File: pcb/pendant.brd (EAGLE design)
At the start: 24 x 99 mm, 47 parts, among them CON1 USB_MICROSMT+THRUHULE, Q2 16MHz, SW2 BUTTON_2, T1 SSM3J328R,LF, T2 SSM3J328R,LF, U2 MK20D--VFM5, U3 74LVC1G17DCK, U4 74LVC1G17DCK

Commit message: Adding support for accelerometer
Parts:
- added TP10, TP11, TP12, TP13, TP14, TP15, TP16, TP9: PTR1B1,27, testpad:B1,27
- R2, R3: value 1k -> 4.7k
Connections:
- net I2C0_SCL: now also TP9.TP
- net I2C0_SDA: now also TP10.TP
- net LED_CLOCK: now also TP11.TP
- net LED_DATA: now also TP12.TP
- net LED_OE: now also TP16.TP
- net LED_S0: now also TP13.TP
- net LED_S1: now also TP14.TP
- net LED_STROBE: now also TP15.TP
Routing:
- net LED_CLOCK: track 16.2 -> 17.5 mm, vias 0 -> 1
- net TMS: track 7.81 -> 8.31 mm
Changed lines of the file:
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@@
 <setting verticaltext="up"/>
 </settings>
-<grid distance="0.5" unitdist="mm" unit="mm" style="lines" multiple="1" display="yes" altdistance="0.25" altunitdist="mm" altunit="mm"/>
+<grid distance="0.5" unitdist="mm" unit="mm" style="lines" multiple="1" display="yes" altdistance="0.1" altunitdist="mm" altunit="mm"/>
 <layers>
 <layer number="1" name="Top" color="4" fill="1" visible="yes" active="yes"/>
@@
 <element name="R1" library="adafruit" package="R0402" value="2000" x="5" y="23" smashed="yes" rot="R90"/>
 <element name="U$6" library="teensy_adapter" package="VFDFN-10" value="MMA8653FC" x="12" y="23" smashed="yes" rot="R180"/>
-<element name="R2" library="adafruit" package="R0402" value="1k" x="9.75" y="20" smashed="yes" rot="R90"/>
-<element name="R3" library="adafruit" package="R0402" value="1k" x="13.25" y="20.75" smashed="yes" rot="R90"/>
+<element name="R2" library="adafruit" package="R0402" value="4.7k" x="9.75" y="20" smashed="yes" rot="R90"/>
+<element name="R3" library="adafruit" package="R0402" value="4.7k" x="13.25" y="20.75" smashed="yes" rot="R90"/>
 <element name="C2" library="adafruit" package="C0402" value="100nF" x="14.75" y="23.75" smashed="yes"/>
 <element name="C3" library="adafruit" package="C0402" value="100nF" x="11.75" y="20.75" smashed="yes" rot="R270"/>
@@
 <element name="U$2" library="blinkinlabs" package="SWITCH_SMD_90_DEGREE" value="SWITCH_SPDT_SHIELD" x="21" y="10.5" smashed="yes" rot="R270">
 <attribute name="VALUE" x="24" y="9.5" size="0.762" layer="27" rot="R270"/>
+</element>
+<element name="TP9" library="testpad" package="B1,27" value="PTR1B1,27" x="14.2" y="22.6" rot="MR0">
+<attribute name="TP_SIGNAL_NAME" value="" x="14.2" y="22.6" size="1.778" layer="28" rot="MR0" display="off"/>
+</element>
+<element name="TP11" library="testpad" package="B1,27" value="PTR1B1,27" x="10.2" y="18.3" rot="MR0">
+<attribute name="TP_SIGNAL_NAME" value="" x="10.2" y="18.3" size="1.778" layer="28" rot="MR0" display="off"/>
+</element>
+<element name="TP12" library="testpad" package="B1,27" value="PTR1B1,27" x="8.9" y="27.8" rot="MR180">
+<attribute name="TP_SIGNAL_NAME" value="" x="8.9" y="27.8" size="1.778" layer="28" rot="MR180" display="off"/>
+</element>
+<element name="TP13" library="testpad" package="B1,27" value="PTR1B1,27" x="9" y="29.3" rot="MR0">
+<attribute name="TP_SIGNAL_NAME" value="" x="9" y="29.3" size="1.778" layer="28" rot="MR0" display="off"/>
+</element>
+<element name="TP14" library="testpad" package="B1,27" value="PTR1B1,27" x="7.1" y="28.1" rot="MR0">
+<attribute name="TP_SIGNAL_NAME" value="" x="7.1" y="28.1" size="1.778" layer="28" rot="MR0" display="off"/>
+</element>
+<element name="TP15" library="testpad" package="B1,27" value="PTR1B1,27" x="6.1" y="18.9" rot="MR0">
+<attribute name="TP_SIGNAL_NAME" value="" x="6.1" y="18.9" size="1.778" layer="28" rot="MR0" display="off"/>
+</element>
+<element name="TP16" library="testpad" package="B1,27" value="PTR1B1,27" x="5.3" y="28.5" rot="MR0">
+<attribute name="TP_SIGNAL_NAME" value="" x="5.3" y="28.5" size="1.778" layer="28" rot="MR0" display="off"/>
+</element>
+<element name="TP10" library="testpad" package="B1,27" value="PTR1B1,27" x="8.7" y="20" rot="MR0">
+<attribute name="TP_SIGNAL_NAME" value="" x="8.7" y="20" size="1.778" layer="28" rot="MR0" display="off"/>
 </element>
 </elements>
@@
 <wire x1="13.25" y1="25.75" x2="13.75" y2="25.25" width="0.254" layer="1"/>
 <wire x1="13.75" y1="25.25" x2="16" y2="25.25" width="0.254" layer="1"/>
+<contactref element="TP16" pad="TP"/>
+<wire x1="5.25" y1="28.5" x2="5.3" y2="28.5" width="0" layer="19" extent="1-16"/>
 </signal>
 <signal name="N$18">
@@
 <wire x1="13.25" y1="18.275" x2="13.25" y2="20.1" width="0.254" layer="1"/>
 <wire x1="14.25" y1="22.6" x2="12.9" y2="22.6" width="0.254" layer="1"/>
+<contactref element="TP9" pad="TP"/>
+<wire x1="14.25" y1="22.6" x2="14.2" y2="22.6" width="0" layer="19" extent="1-16"/>
 </signal>
 <signal name="I2C0_SDA">
@@
 <wire x1="12.75" y1="19" x2="12.5" y2="19.25" width="0.254" layer="1"/>
 <wire x1="11.1" y1="22.2" x2="10.7" y2="22.2" width="0.254" layer="1"/>
-<via x="10.5" y="21.5" extent="1-16" drill="0.35"/>
-<wire x1="10.5" y1="21.5" x2="10.25" y2="21.5" width="0.254" layer="16"/>
 <wire x1="10.25" y1="21.5" x2="8.75" y2="20" width="0.254" layer="16"/>
 <via x="8.75" y="20" extent="1-16" drill="0.35"/>
@@
 <wire x1="8.75" y1="19.75" x2="9.15" y2="19.35" width="0.254" layer="1"/>
 <wire x1="9.85" y1="19.25" x2="9.75" y2="19.35" width="0.254" layer="1"/>
+<via x="10.5" y="21.5" extent="1-16" drill="0.35"/>
+<wire x1="10.5" y1="21.5" x2="10.25" y2="21.5" width="0.254" layer="16"/>
+<contactref element="TP10" pad="TP"/>
+<wire x1="8.7" y1="20" x2="8.75" y2="20" width="0.254" layer="16"/>
 </signal>
 <signal name="N$8">
@@
 <wire x1="20.5" y1="17.25" x2="20.45" y2="17.3" width="0.254" layer="1"/>
 <wire x1="20.45" y1="17.3" x2="20.45" y2="19.05" width="0.254" layer="1"/>
-<wire x1="21.25" y1="18" x2="21.5" y2="17.75" width="0" layer="19" extent="16-16"/>
+<wire x1="21.5" y1="17.75" x2="21" y2="17.75" width="0.254" layer="16"/>
 </signal>
 <signal name="RX">
@@
 <wire x1="9" y1="28" x2="7.5" y2="26.5" width="0.254" layer="1"/>
 <wire x1="11" y1="28" x2="9" y2="28" width="0.254" layer="16"/>
+<contactref element="TP12" pad="TP"/>
+<wire x1="8.9" y1="27.8" x2="9" y2="27.9" width="0.254" layer="16"/>
+<wire x1="9" y1="27.9" x2="9" y2="28" width="0.254" layer="16"/>
 </signal>
 <signal name="LED_CLOCK">
@@
 <wire x1="8" y1="25.75" x2="8" y2="19.75" width="0.254" layer="1"/>
 <wire x1="8" y1="19.75" x2="9.25" y2="18.5" width="0.254" layer="1"/>
-<wire x1="9.25" y1="18.5" x2="9.25" y2="17" width="0.254" layer="1"/>
+<wire x1="9.25" y1="18.5" x2="9.25" y2="18.3" width="0.254" layer="1"/>
+<wire x1="9.25" y1="18.3" x2="9.25" y2="17" width="0.254" layer="1"/>
 <wire x1="9.25" y1="17" x2="9.5" y2="16.75" width="0.254" layer="1"/>
 <wire x1="9.5" y1="16.75" x2="10.225" y2="16.75" width="0.254" layer="1"/>
@@
 <wire x1="10.25" y1="28" x2="10.25" y2="28.5" width="0.254" layer="1"/>
 <wire x1="10.25" y1="28.5" x2="10.75" y2="29" width="0.254" layer="1"/>
+<contactref element="TP11" pad="TP"/>
+<wire x1="10.4" y1="18.5" x2="10.2" y2="18.3" width="0.254" layer="16"/>
+<via x="10.2" y="18.3" extent="1-16" drill="0.35"/>
+<wire x1="10.2" y1="18.3" x2="10" y2="18.3" width="0.254" layer="1"/>
+<wire x1="10" y1="18.3" x2="9.25" y2="18.3" width="0.254" layer="1"/>
 </signal>
 <signal name="LED_STROBE">
@@
 <wire x1="7.75" y1="15.25" x2="8" y2="15.25" width="0.254" layer="1"/>
 <wire x1="8" y1="15.25" x2="9" y2="14.25" width="0.254" layer="1"/>
+<contactref element="TP15" pad="TP"/>
+<wire x1="6.1" y1="18.9" x2="6" y2="18.8" width="0.254" layer="16"/>
+<wire x1="6" y1="18.8" x2="6" y2="18.5" width="0.254" layer="16"/>
 </signal>
 <signal name="LED_S0">
@@
 <wire x1="18" y1="26.4" x2="18.15" y2="26.25" width="0.254" layer="1"/>
 <wire x1="18.15" y1="26.25" x2="18" y2="26.25" width="0.254" layer="1"/>
+<contactref element="TP13" pad="TP"/>
+<wire x1="9" y1="29.3" x2="9" y2="29" width="0.254" layer="16"/>
 </signal>
 <signal name="LED_S1">
@@
 <wire x1="14.5" y1="26.75" x2="14.5" y2="26.65" width="0.254" layer="1"/>
 <wire x1="14.5" y1="26.65" x2="14.1" y2="26.25" width="0.254" layer="1"/>
+<contactref element="TP14" pad="TP"/>
+<wire x1="7.1" y1="28.1" x2="6.875" y2="27.875" width="0.254" layer="16"/>
 </signal>
 <signal name="N$6">

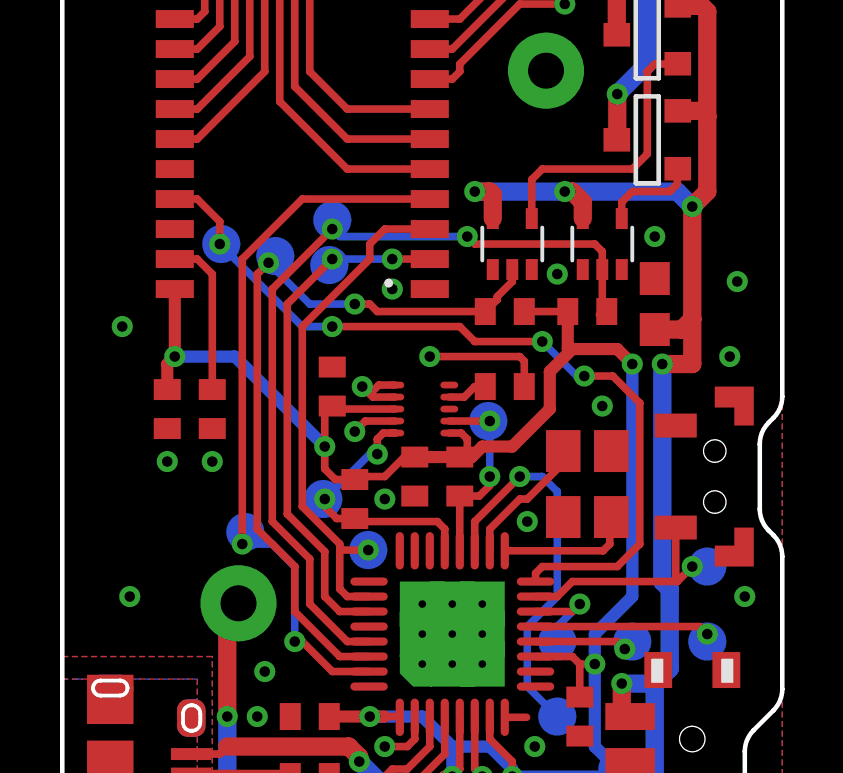
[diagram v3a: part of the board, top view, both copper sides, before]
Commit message: Add interrupt line from accelerometer, clean up test pad positions
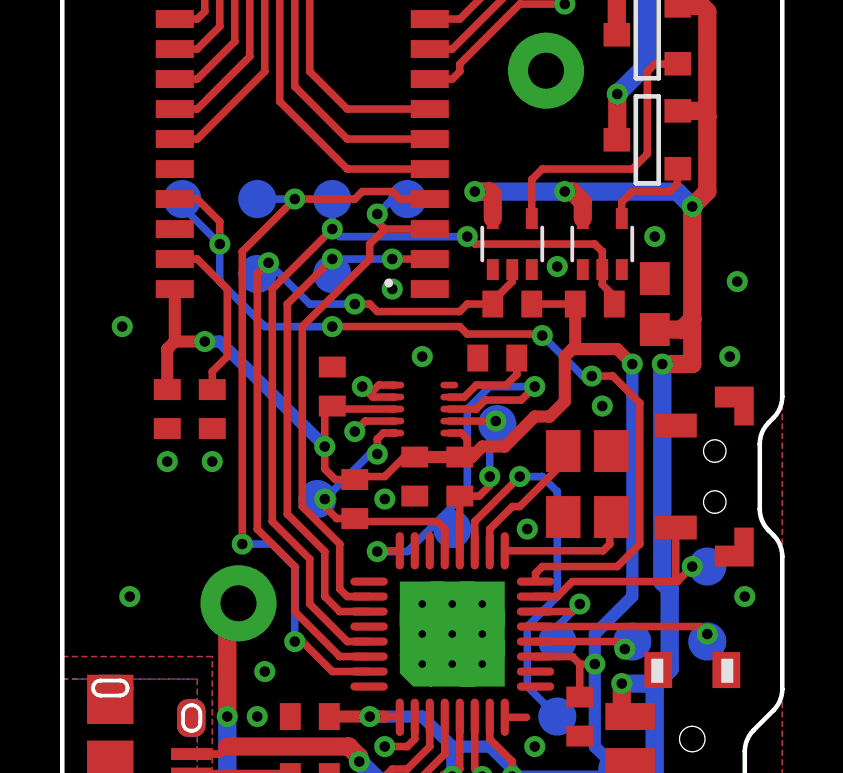
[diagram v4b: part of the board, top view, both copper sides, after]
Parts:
- added TP17: PTR1B1,27, testpad:B1,27
- moved TP11 11.8 mm to (11.5, 30.0)
- moved TP15 11.1 mm to (6.50, 30.0)
- moved TP16 1.98 mm to (4.00, 30.0)
- moved C2 0.98 mm to (14.5, 24.7), turned to 180 degrees
- moved TP14 0.85 mm to (6.50, 27.5)
- moved TP13 0.70 mm to (9.00, 30.0)
- moved R4 0.35 mm to (15.0, 26.5)
- moved R5 0.35 mm to (17.8, 26.5)
- moved TP9 0.32 mm to (14.5, 22.5)
- moved TP12 0.32 mm to (9.00, 27.5)
- moved TP10 0.20 mm to (8.50, 20.0)
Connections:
- removed net INT1: U$6.P$3
- removed net INT2: U$6.P$5
- new net ACC_INT1: TP17.TP, U$6.P$3, U2.24
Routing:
- net ACC_INT1: track 0.00 -> 13.6 mm, vias 0 -> 2
- net GND: track 12.6 -> 8.53 mm
- net LED_OE: track 27.6 -> 30.4 mm
- net N$4: track 1.34 -> 3.11 mm
- net LED_STROBE: track 24.5 -> 25.6 mm, vias 2 -> 3
- net LED_CLOCK: track 17.5 -> 18.0 mm
